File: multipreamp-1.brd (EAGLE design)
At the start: 100 x 50 mm, 140 parts, among them Q1 J201, Q2 J201, Q3 J201, Q4 J201, Q5 J201, Q6 J201, Q7 J201, Q8 2N5088

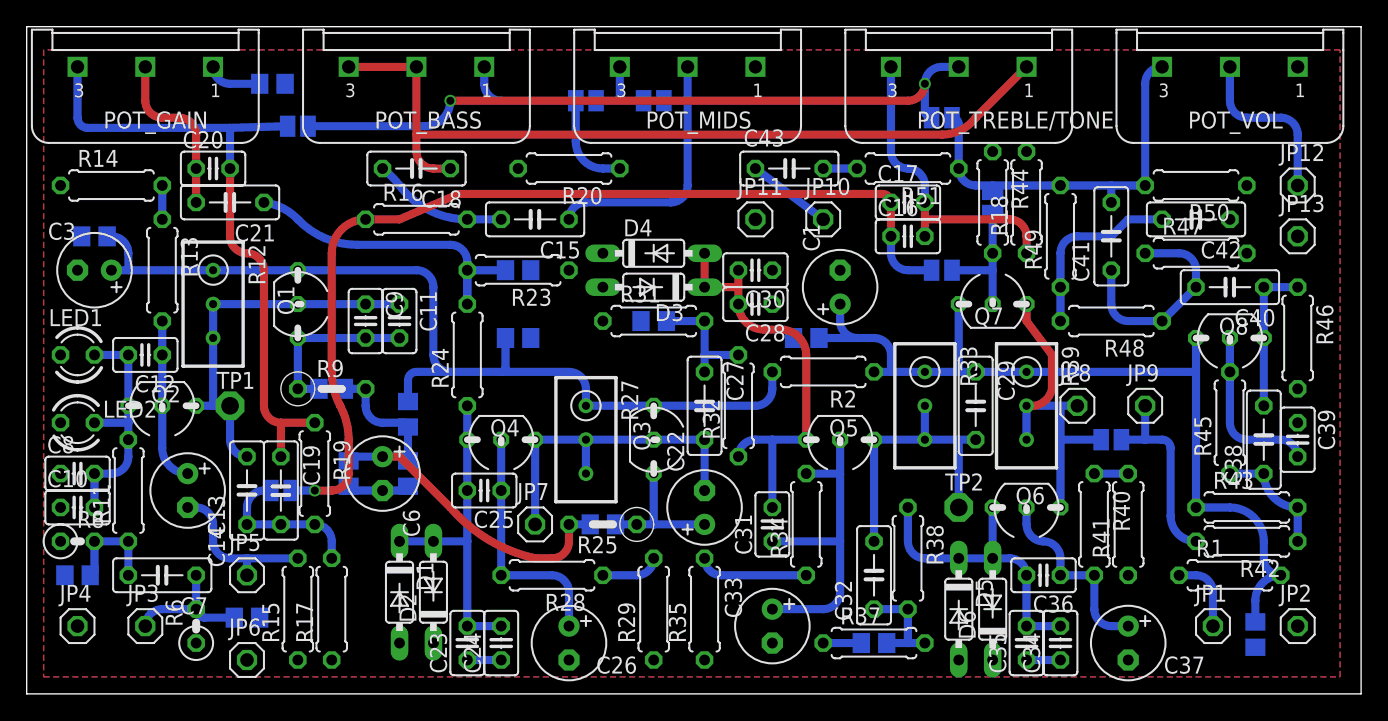
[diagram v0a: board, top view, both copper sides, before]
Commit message: Ajustes no esquematico e layout - Adicao de capacitor em serie com buffer FET de saida, ajuste de posicionamento de labels, adicao de vias
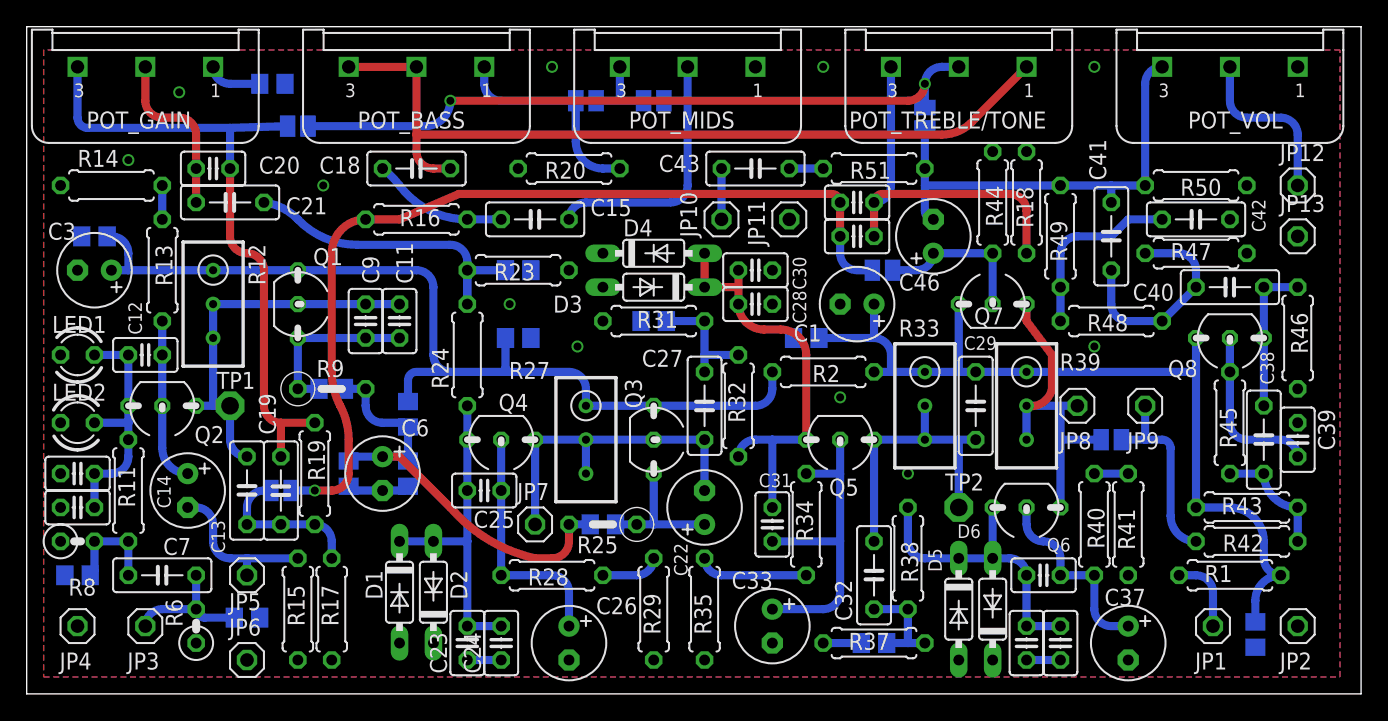
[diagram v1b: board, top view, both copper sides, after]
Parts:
- removed SJ7: (no value), jumper:SJ
- added C46: (no value), rcl:E2,5-6
- moved JP10 7.62 mm to (52.1, 35.6)
- moved SJ8 4.44 mm to (64.1, 31.8)
- moved C16 3.81 mm to (62.2, 34.3)
- moved C17 3.81 mm to (62.2, 36.8)
- moved R51 2.54 mm to (63.5, 39.4)
- moved C43 2.54 mm to (54.6, 39.4)
- moved JP11 2.54 mm to (57.1, 35.6)
- moved C1 1.80 mm to (62.2, 29.2), turned to 180 degrees
- moved SJ6 1.27 mm to (67.3, 43.2), turned to 270 degrees
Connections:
- net N$45: now also C46.+; no longer SJ7.1
- net N$9: now also C46.-; no longer SJ7.2
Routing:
- net TONE/TREBLE_3: track 23.2 -> 28.6 mm
- net N$9: track 29.7 -> 34.3 mm
- net TONE_IN: track 72.5 -> 68.1 mm
- net N$14: track 6.35 -> 3.81 mm
- net N$45: track 9.91 -> 11.8 mm
- net TONE_OUT: track 53.4 -> 52.4 mm
- net V+/2: track 65.7 -> 65.1 mm
- net GND: vias 0 -> 11

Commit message: Ajustes finais no layout e esquematico - posicionamento de labels, troca de testpoints por pinheads, adicao de assinatura na placa Gerber v1.0 gerado com base nessa versao
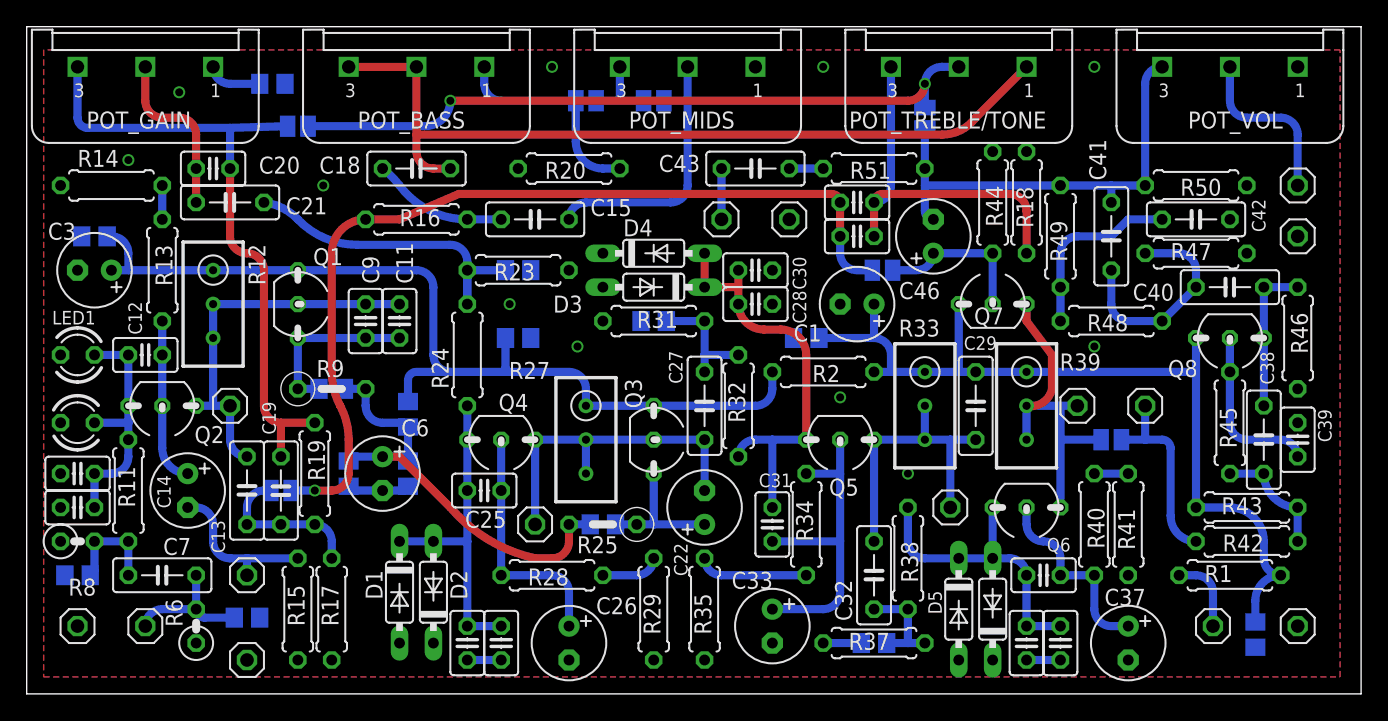
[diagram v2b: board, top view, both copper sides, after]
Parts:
- removed TP1, TP2: PTR1PAD1-13, testpad:P1-13
- added JP14: P1, pinhead:1X01
- added JP15: P3, pinhead:1X01
- JP1: value (none) -> V+
- JP10: value (none) -> PRES
- JP11, JP13, JP2, JP4, JP6: value (none) -> GND
- JP12: value (none) -> OUT
- JP3: value (none) -> IN
- JP5: value (none) -> SW
- JP7: value (none) -> P2
- JP8: value (none) -> P4
- JP9: value (none) -> P5
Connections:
- net N$22: now also JP15.1; no longer TP2.TP
- net N$8: now also JP14.1; no longer TP1.TP
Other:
- board text added: "03/2016"
- board text added: "MULTIPREAMP v1.0"
- board text added: "PTSK"
